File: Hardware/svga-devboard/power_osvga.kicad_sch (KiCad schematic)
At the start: 68 parts

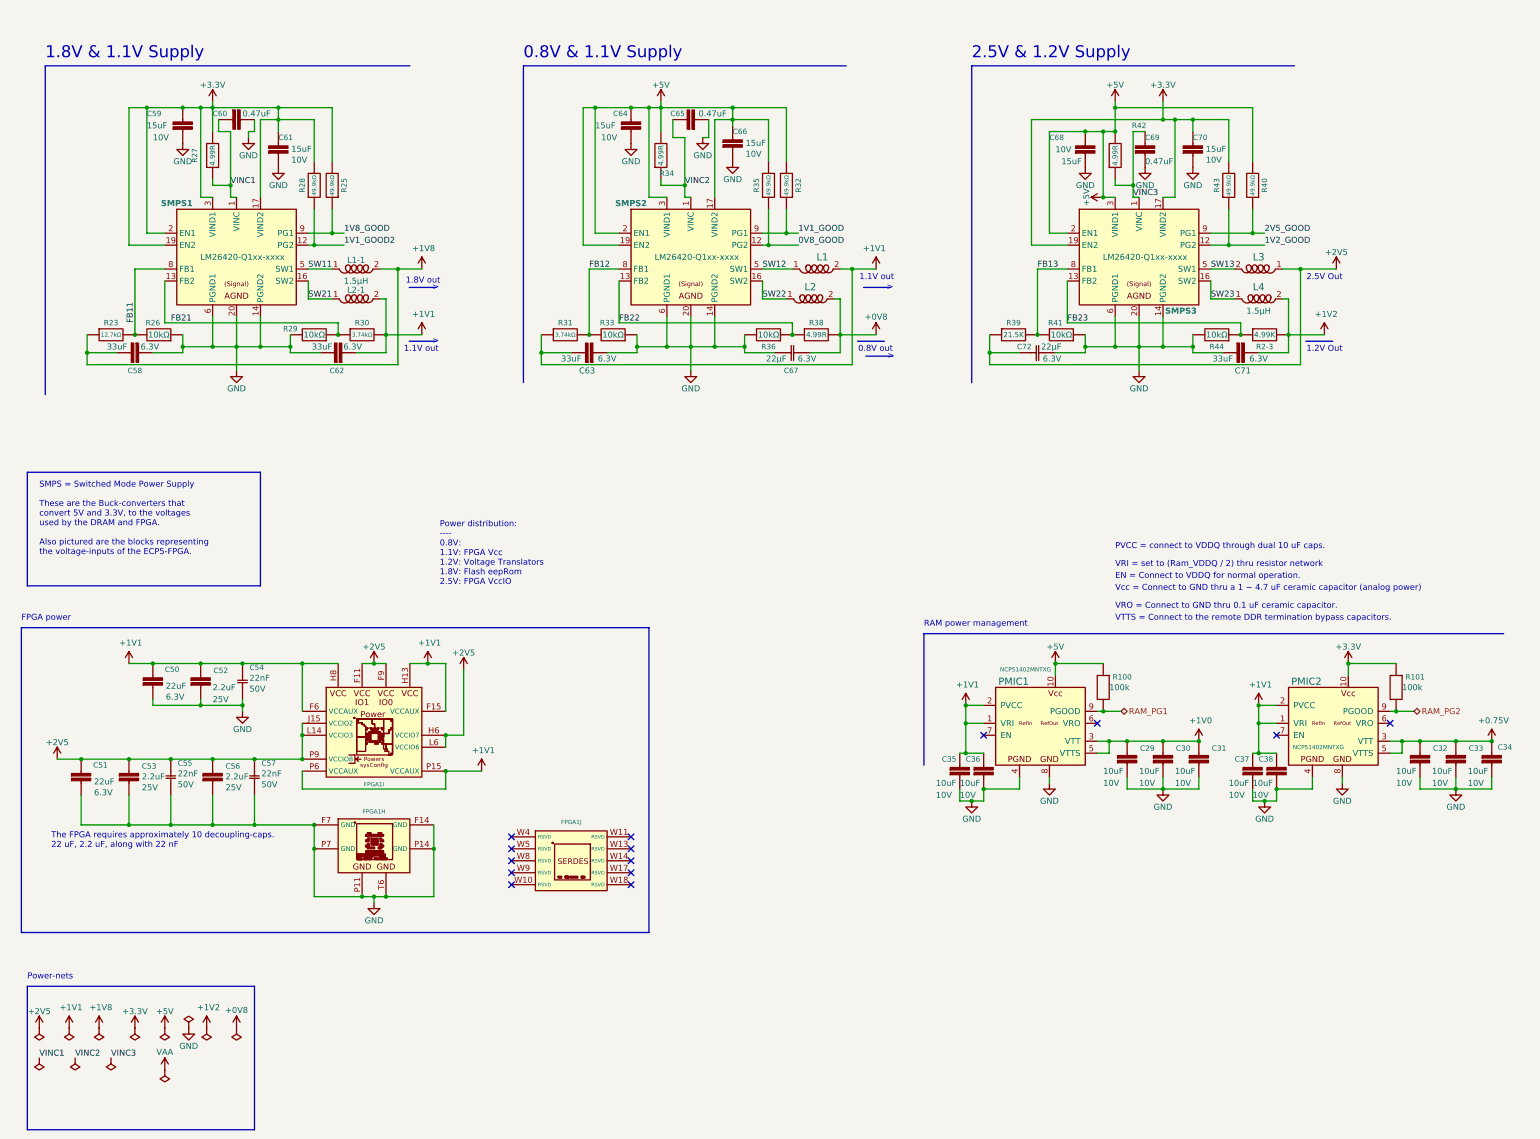
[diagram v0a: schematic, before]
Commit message: Disconnected the DVI-connectors from each other, so that they do go over the intended flat-cable to the daughter-board instead.
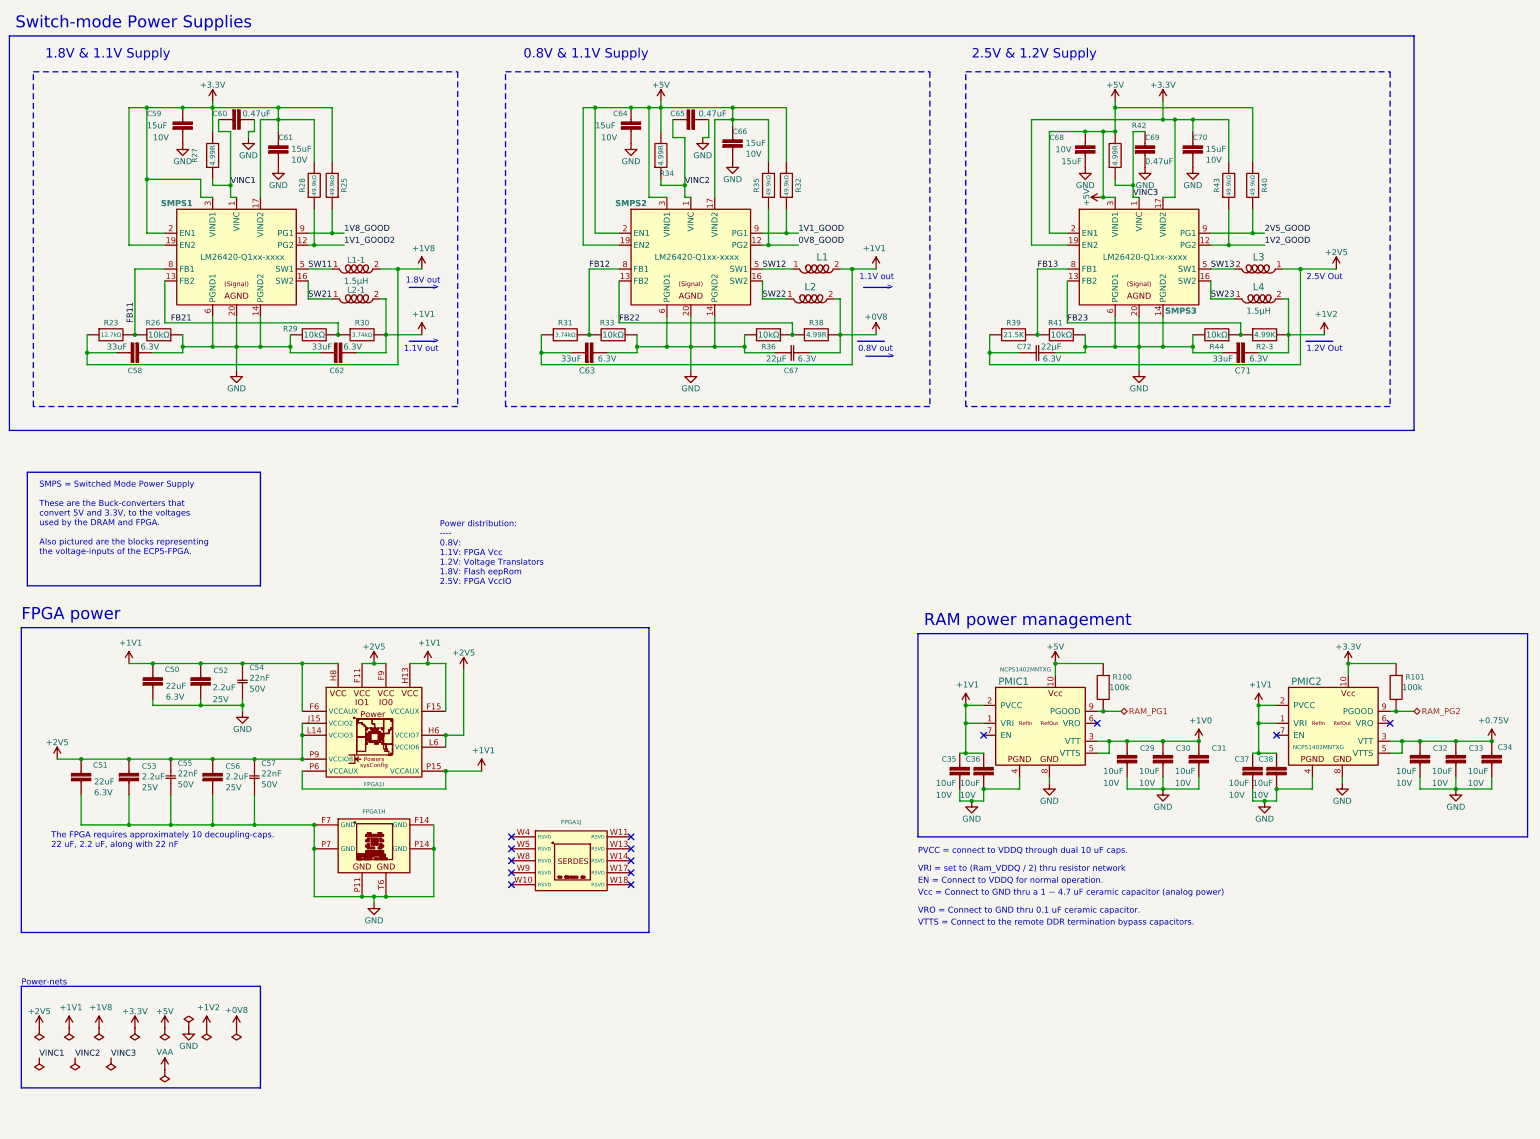
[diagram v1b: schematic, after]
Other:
- note added: "Switch-mode Power Supplies"
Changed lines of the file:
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@@
   (junction (at 95.25 67.31) (diameter 0) (color 0 0 0 0)
   )
+  (junction (at 55.88 55.88) (diameter 0) (color 0 0 0 0)
+  )
   (junction (at 260.35 175.26) (diameter 0) (color 0 0 0 0)
   )
@@
   )
   (junction (at 229.87 171.45) (diameter 0) (color 0 0 0 0)
-  )
-  (junction (at 67.31 40.64) (diameter 0) (color 0 0 0 0)
   )
   (junction (at 261.62 40.64) (diameter 0) (color 0 0 0 0)
@@
     (stroke (width 0) (type default))
   )
+  (wire (pts (xy 55.88 55.88) (xy 55.88 67.31))
+    (stroke (width 0) (type default))
+  )
   (wire (pts (xy 162.56 40.64) (xy 162.56 59.69))
     (stroke (width 0) (type default))
@@
     (stroke (width 0) (type default))
   )
-  (polyline (pts (xy 299.72 31.75) (xy 231.14 31.75))
-    (stroke (width 0) (type default))
-  )
   (wire (pts (xy 78.74 193.04) (xy 91.44 193.04))
     (stroke (width 0) (type default))
@@
     (stroke (width 0) (type default))
   )
-  (wire (pts (xy 63.5 40.64) (xy 67.31 40.64))
-    (stroke (width 0) (type default))
-  )
   (wire (pts (xy 59.69 86.36) (xy 59.69 77.47))
     (stroke (width 0) (type default))
@@
     (stroke (width 0) (type default))
   )
-  (polyline (pts (xy 78.74 257.81) (xy 78.74 227.33))
+  (polyline (pts (xy 80.01 248.92) (xy 80.01 227.33))
     (stroke (width 0) (type default))
   )
@@
     (stroke (width 0) (type default))
   )
-  (polyline (pts (xy 30.48 227.33) (xy 30.48 257.81))
+  (polyline (pts (xy 29.21 227.33) (xy 29.21 248.92))
     (stroke (width 0) (type default))
   )
@@
     (stroke (width 0) (type default))
   )
-  (polyline (pts (xy 34.29 31.75) (xy 34.29 101.6))
-    (stroke (width 0) (type default))
-  )
   (wire (pts (xy 104.14 208.28) (xy 101.6 208.28))
     (stroke (width 0) (type default))
@@
     (stroke (width 0) (type default))
   )
+  (wire (pts (xy 67.31 55.88) (xy 55.88 55.88))
+    (stroke (width 0) (type default))
+  )
   (wire (pts (xy 52.07 158.75) (xy 57.15 158.75))
     (stroke (width 0) (type default))
@@
     (stroke (width 0) (type default))
   )
-  (polyline (pts (xy 30.48 257.81) (xy 78.74 257.81))
+  (polyline (pts (xy 29.21 248.92) (xy 80.01 248.92))
     (stroke (width 0) (type default))
   )
@@
     (stroke (width 0) (type default))
   )
-  (polyline (pts (xy 231.14 31.75) (xy 231.14 99.06))
-    (stroke (width 0) (type default))
-  )
   (wire (pts (xy 271.78 182.88) (xy 271.78 185.42))
     (stroke (width 0) (type default))
@@
     (stroke (width 0) (type default))
   )
+  (wire (pts (xy 67.31 59.69) (xy 67.31 55.88))
+    (stroke (width 0) (type default))
+  )
   (wire (pts (xy 67.31 167.64) (xy 76.2 167.64))
     (stroke (width 0) (type default))
@@
     (stroke (width 0) (type default))
   )
-  (polyline (pts (xy 220.98 152.4) (xy 220.98 180.34))
-    (stroke (width 0) (type default))
-  )
-  (wire (pts (xy 67.31 40.64) (xy 69.85 40.64))
+  (wire (pts (xy 63.5 40.64) (xy 69.85 40.64))
     (stroke (width 0) (type default))
   )
@@
     (stroke (width 0) (type default))
   )
-  (polyline (pts (xy 78.74 227.33) (xy 30.48 227.33))
+  (polyline (pts (xy 80.01 227.33) (xy 29.21 227.33))
     (stroke (width 0) (type default))
   )
@@
     (stroke (width 0) (type default))
   )
-  (wire (pts (xy 55.88 40.64) (xy 55.88 67.31))
+  (wire (pts (xy 55.88 40.64) (xy 55.88 55.88))
     (stroke (width 0) (type default))
   )
@@
     (stroke (width 0) (type default))
   )
-  (wire (pts (xy 67.31 40.64) (xy 67.31 59.69))
-    (stroke (width 0) (type default))
-  )
   (wire (pts (xy 88.9 181.61) (xy 88.9 185.42))
     (stroke (width 0) (type default))
@@
     (stroke (width 0) (type default))
   )
-  (polyline (pts (xy 135.89 31.75) (xy 135.89 99.06))
-    (stroke (width 0) (type default))
-  )
   (wire (pts (xy 264.16 185.42) (xy 271.78 185.42))
     (stroke (width 0) (type default))
@@
     (stroke (width 0) (type default))
   )
-  (polyline (pts (xy 111.76 31.75) (xy 34.29 31.75))
-    (stroke (width 0) (type default))
-  )
   (wire (pts (xy 88.9 185.42) (xy 119.38 185.42))
     (stroke (width 0) (type default))
@@
     (stroke (width 0) (type default))
   )
-  (polyline (pts (xy 204.47 31.75) (xy 135.89 31.75))
-    (stroke (width 0) (type default))
-  )
   (wire (pts (xy 71.12 45.72) (xy 71.12 43.18))
     (stroke (width 0) (type default))
@@
     (stroke (width 0) (type default))
   )
-  (polyline (pts (xy 344.17 152.4) (xy 220.98 152.4))
-    (stroke (width 0) (type default))
-  )
   (polyline (pts (xy 80.01 142.24) (xy 30.48 142.24))
     (stroke (width 0) (type default))
@@
   (wire (pts (xy 69.85 57.15) (xy 73.66 57.15))
     (stroke (width 0) (type default))
+  )
+  (rectangle (start 219.71 152.4) (end 349.25 195.58)
+    (stroke (width 0) (type default))
+    (fill (type none))
+  )
+  (rectangle (start 132.08 33.02) (end 222.25 104.14)
+    (stroke (width 0) (type dash))
+    (fill (type none))
+  )
+  (rectangle (start 229.87 33.02) (end 320.04 104.14)
+    (stroke (width 0) (type dash))
+    (fill (type none))
+  )
+  (rectangle (start 31.75 33.02) (end 121.92 104.14)
+    (stroke (width 0) (type dash))
+    (fill (type none))
+  )
+  (rectangle (start 26.67 25.4) (end 325.12 109.22)
+    (stroke (width 0) (type default))
+    (fill (type none))
   )
   (text "1.1V out" (at 214.63 77.47 0)
@@
   )
   (text "VRO = Connect to GND thru 0.1 uF ceramic capacitor."
-    (at 261.62 147.32 0)
+    (at 219.71 212.09 0)
     (effects (font (size 1.27 1.27)) (justify left bottom))
   )
   (text "VTTS = Connect to the remote DDR termination bypass capacitors."
-    (at 261.62 149.86 0)
+    (at 219.71 214.63 0)
     (effects (font (size 1.27 1.27)) (justify left bottom))
   )
@@
     (effects (font (size 1.27 1.27)) (justify left bottom))
   )
-  (text "VRI = set to (Ram_VDDQ / 2) thru resistor network" (at 261.62 138.43 0)
+  (text "VRI = set to (Ram_VDDQ / 2) thru resistor network" (at 219.71 203.2 0)
     (effects (font (size 1.27 1.27)) (justify left bottom))
   )
@@
     (effects (font (size 1.27 1.27)) (justify right bottom))
   )
-  (text "EN = Connect to VDDQ for normal operation." (at 261.62 140.97 0)
+  (text "EN = Connect to VDDQ for normal operation." (at 219.71 205.74 0)
     (effects (font (size 1.27 1.27)) (justify left bottom))
   )
@@
   )
   (text "1.8V & 1.1V Supply" (at 34.29 30.48 0)
+    (effects (font (size 2 2)) (justify left bottom))
+  )
+  (text "Switch-mode Power Supplies" (at 27.94 24.13 0)
     (effects (font (size 2.54 2.54)) (justify left bottom))
   )
   (text "2.5V & 1.2V Supply\n" (at 231.14 30.48 0)
+    (effects (font (size 2 2)) (justify left bottom))
+  )
+  (text ">" (at 213.233 94.234 0)
+    (effects (font (size 1.27 1.27)) (justify left bottom))
+  )
+  (text "0.8V & 1.1V Supply\n" (at 135.89 30.48 0)
+    (effects (font (size 2 2)) (justify left bottom))
+  )
+  (text "Power-nets" (at 29.21 227.33 0)
+    (effects (font (size 1.27 1.27)) (justify left bottom))
+  )
+  (text "1.1V out" (at 110.49 92.71 0)
+    (effects (font (size 1.27 1.27)) (justify left bottom))
+  )
+  (text "PVCC = connect to VDDQ through dual 10 uF caps." (at 219.71 199.39 0)
+    (effects (font (size 1.27 1.27)) (justify left bottom))
+  )
+  (text "RAM power management" (at 220.98 151.13 0)
     (effects (font (size 2.54 2.54)) (justify left bottom))
   )
-  (text ">" (at 213.233 94.234 0)
-    (effects (font (size 1.27 1.27)) (justify left bottom))
-  )
-  (text "0.8V & 1.1V Supply\n" (at 135.89 30.48 0)
+  (text "Vcc = Connect to GND thru a 1 − 4.7 uF ceramic capacitor (analog power)"
+    (at 219.71 208.28 0)
+    (effects (font (size 1.27 1.27)) (justify left bottom))
+  )
+  (text "FPGA power" (at 29.21 149.86 0)
     (effects (font (size 2.54 2.54)) (justify left bottom))
   )
-  (text "Power-nets" (at 30.48 226.06 0)
-    (effects (font (size 1.27 1.27)) (justify left bottom))
-  )
-  (text "1.1V out" (at 110.49 92.71 0)
-    (effects (font (size 1.27 1.27)) (justify left bottom))
-  )
-  (text "PVCC = connect to VDDQ through dual 10 uF caps." (at 261.62 134.62 0)
-    (effects (font (size 1.27 1.27)) (justify left bottom))
-  )
-  (text "RAM power management" (at 220.98 151.13 0)
-    (effects (font (size 1.27 1.27)) (justify left bottom))
-  )
-  (text "Vcc = Connect to GND thru a 1 − 4.7 uF ceramic capacitor (analog power)"
-    (at 261.62 143.51 0)
-    (effects (font (size 1.27 1.27)) (justify left bottom))
-  )
-  (text "FPGA power" (at 29.21 149.86 0)
-    (effects (font (size 1.27 1.27)) (justify left bottom))
-  )
   (label "2V5_GOOD" (at 293.37 67.31 0) (fields_autoplaced)
